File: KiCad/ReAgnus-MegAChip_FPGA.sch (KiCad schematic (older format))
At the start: 13 parts, among them J2 Conn_02x05_Odd_Even, J3 Conn_02x02_Odd_Even, U1 GW1NR-UV9LQ144P, U10 74LVC245A, U9 74LVC1GX04, Y1 CL=16pF

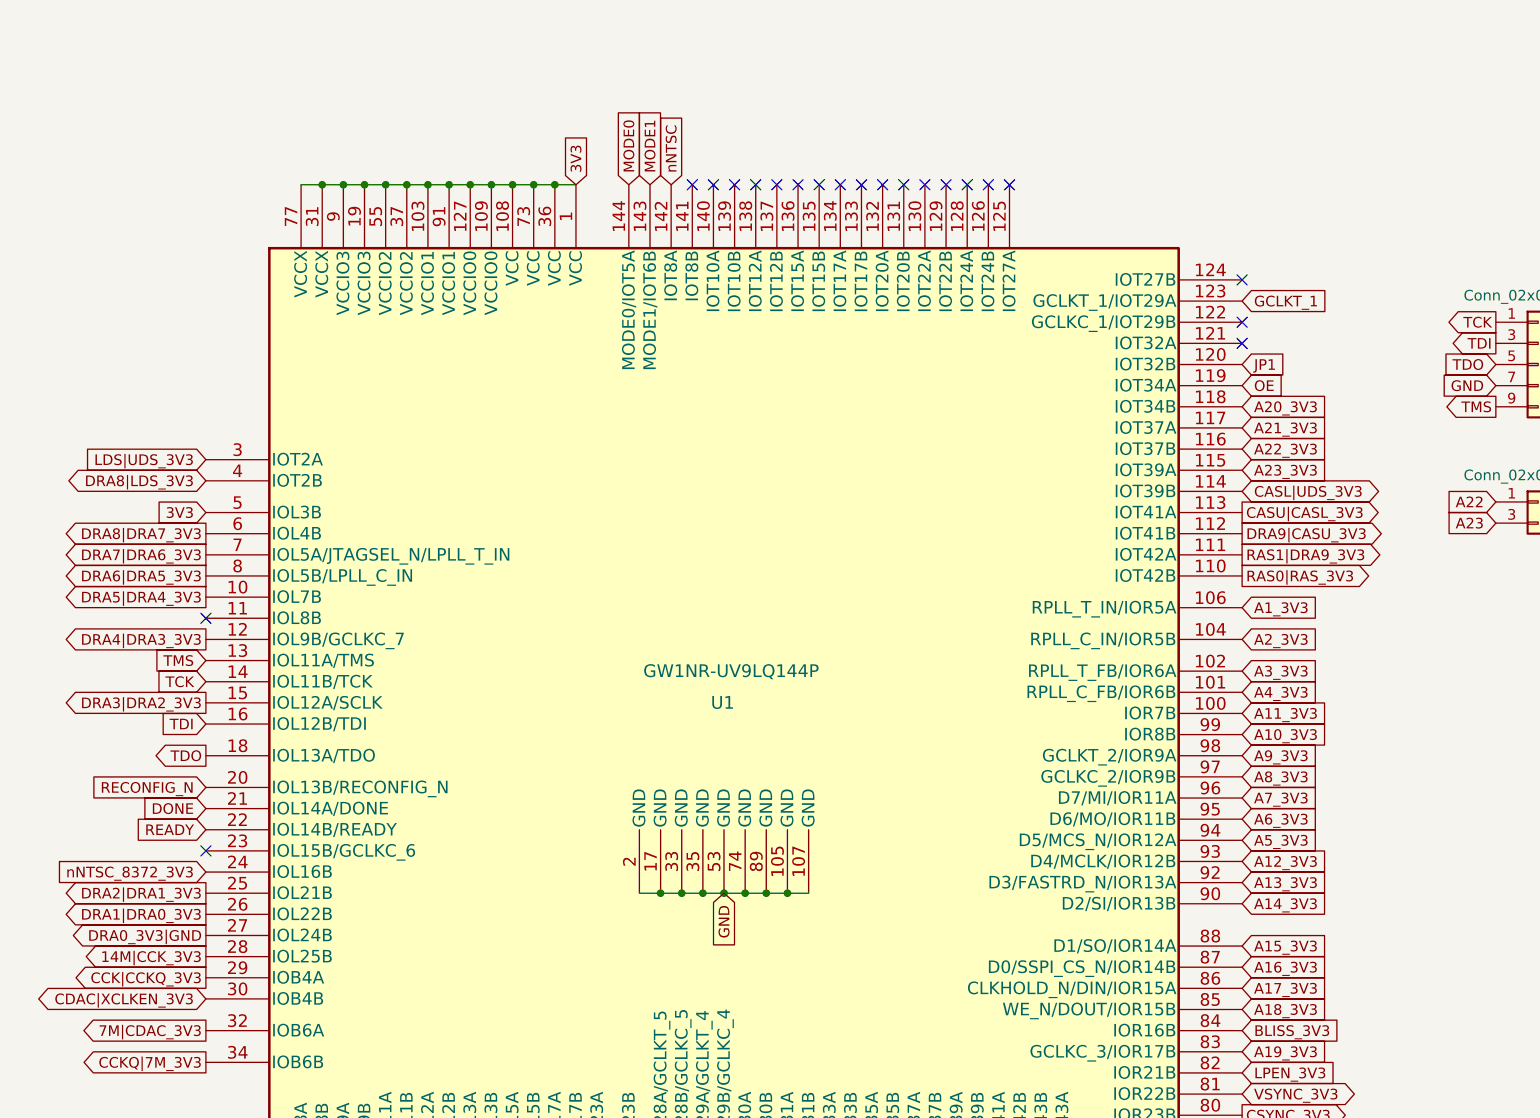
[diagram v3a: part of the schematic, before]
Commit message: Moved signals from bank 3 to bank 0
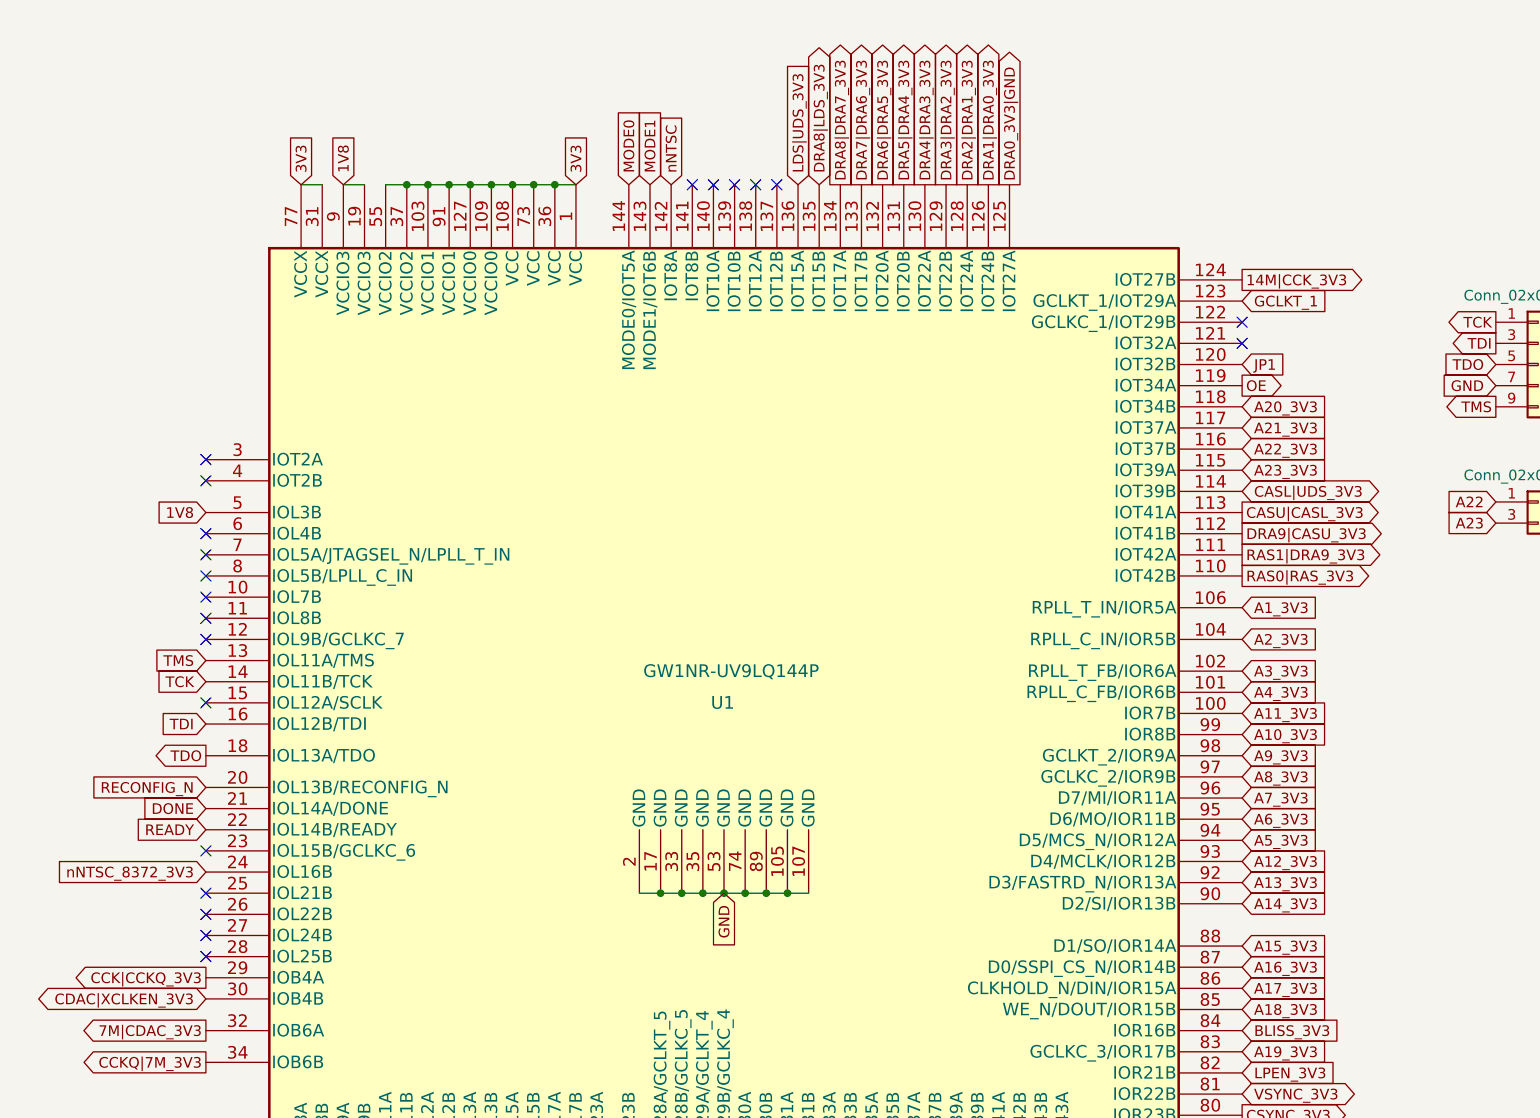
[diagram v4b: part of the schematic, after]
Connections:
- net 14M|CCK_3V3: now also U1.124 (IOT27B); no longer U1.28 (IOL25B)
- net 3V3: no longer U1.19 (VCCIO3), U1.5 (IOL3B), U1.9 (VCCIO3)
- net DRA0_3V3|GND: now also U1.125 (IOT27A); no longer U1.27 (IOL24B)
- net DRA1|DRA0_3V3: now also U1.126 (IOT24B); no longer U1.26 (IOL22B)
- net DRA2|DRA1_3V3: now also U1.128 (IOT24A); no longer U1.25 (IOL21B)
- net DRA3|DRA2_3V3: now also U1.129 (IOT22B); no longer U1.15 (IOL12A/SCLK)
- net DRA4|DRA3_3V3: now also U1.130 (IOT22A); no longer U1.12 (IOL9B/GCLKC_7)
- net DRA5|DRA4_3V3: now also U1.131 (IOT20B); no longer U1.10 (IOL7B)
- net DRA6|DRA5_3V3: now also U1.132 (IOT20A); no longer U1.8 (IOL5B/LPLL_C_IN)
- net DRA7|DRA6_3V3: now also U1.133 (IOT17B); no longer U1.7 (IOL5A/JTAGSEL_N/LPLL_T_IN)
- net DRA8|DRA7_3V3: now also U1.134 (IOT17A); no longer U1.6 (IOL4B)
- net DRA8|LDS_3V3: now also U1.135 (IOT15B); no longer U1.4 (IOT2B)
- net LDS|UDS_3V3: now also U1.136 (IOT15A); no longer U1.3 (IOT2A)
- new net 1V8: U1.19 (VCCIO3), U1.5 (IOL3B), U1.9 (VCCIO3)
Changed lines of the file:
@@
 Text GLabel 6400 2300 2    50   BiDi ~ 0
 CASL|UDS_3V3
-Text GLabel 1500 3000 0    50   Output ~ 0
+Text GLabel 4900 850  1    50   Output ~ 0
 DRA4|DRA3_3V3
-Text GLabel 1500 3300 0    50   Output ~ 0
+Text GLabel 5000 850  1    50   Output ~ 0
 DRA3|DRA2_3V3
-Text GLabel 1500 4200 0    50   Output ~ 0
+Text GLabel 5100 850  1    50   Output ~ 0
 DRA2|DRA1_3V3
-Text GLabel 1500 4300 0    50   Output ~ 0
+Text GLabel 5200 850  1    50   Output ~ 0
 DRA1|DRA0_3V3
-Text GLabel 1500 4400 0    50   Output ~ 0
+Text GLabel 5300 850  1    50   Output ~ 0
 DRA0_3V3|GND
 Text GLabel 2450 5750 3    50   Output ~ 0
@@
 Text GLabel 1500 4600 0    50   Output ~ 0
 CCK|CCKQ_3V3
-Text GLabel 1500 4500 0    50   Output ~ 0
+Text GLabel 6400 1300 2    50   Output ~ 0
 14M|CCK_3V3
 Text GLabel 1500 4850 0    50   Output ~ 0
@@
 Wire Wire Line
 	1950 850  2050 850
-Connection ~ 2050 850
-Wire Wire Line
-	2050 850  2150 850
-Connection ~ 2150 850
-Wire Wire Line
-	2150 850  2250 850
-Connection ~ 2250 850
-Wire Wire Line
-	2250 850  2350 850
-Connection ~ 2350 850
 Wire Wire Line
 	2350 850  2450 850
@@
 GND
 Text GLabel 1500 2400 0    50   Input ~ 0
-3V3
+1V8
 Text GLabel 3850 5750 3    50   Input ~ 0
 XCLK|A20_3V3
-Text GLabel 1500 2150 0    50   Input ~ 0
+Text GLabel 4300 850  1    50   Input ~ 0
 LDS|UDS_3V3
-Text GLabel 1500 2250 0    50   BiDi ~ 0
+Text GLabel 4400 850  1    50   BiDi ~ 0
 DRA8|LDS_3V3
-Text GLabel 1500 2500 0    50   Output ~ 0
+Text GLabel 4500 850  1    50   Output ~ 0
 DRA8|DRA7_3V3
-Text GLabel 1500 2600 0    50   Output ~ 0
+Text GLabel 4600 850  1    50   Output ~ 0
 DRA7|DRA6_3V3
-Text GLabel 1500 2700 0    50   Output ~ 0
+Text GLabel 4700 850  1    50   Output ~ 0
 DRA6|DRA5_3V3
-Text GLabel 1500 2800 0    50   Output ~ 0
+Text GLabel 4800 850  1    50   Output ~ 0
 DRA5|DRA4_3V3
 Text GLabel 9000 1450 3    50   Input ~ 0
@@
 	0    -1   -1   0
 $EndComp
-Text GLabel 6400 1800 2    50   Input ~ 0
+Text GLabel 6400 1800 2    50   Output ~ 0
 OE
 Wire Wire Line
@@
 Wire Wire Line
 	6350 7650 6450 7650
-NoConn ~ 6400 1600
-NoConn ~ 6400 1500
-NoConn ~ 6400 1300
-NoConn ~ 5300 850
-NoConn ~ 5200 850
-NoConn ~ 5100 850
-NoConn ~ 5000 850
-NoConn ~ 4900 850
-NoConn ~ 4800 850
-NoConn ~ 4700 850
-NoConn ~ 4600 850
-NoConn ~ 4500 850
-NoConn ~ 4400 850
-NoConn ~ 4300 850
 NoConn ~ 4200 850
 NoConn ~ 4100 850
@@
 NoConn ~ 1500 4000
 NoConn ~ 1500 2900
+NoConn ~ 1500 4500
+NoConn ~ 1500 4400
+NoConn ~ 1500 4300
+NoConn ~ 1500 4200
+Text GLabel 2150 850  1    50   Input ~ 0
+1V8
+Wire Wire Line
+	2150 850  2250 850
+Text GLabel 1950 850  1    50   Input ~ 0
+3V3
+NoConn ~ 1500 2150
+NoConn ~ 1500 2250
+NoConn ~ 1500 2500
+NoConn ~ 1500 2600
+NoConn ~ 1500 2700
+NoConn ~ 1500 3300
+NoConn ~ 1500 2800
+NoConn ~ 1500 3000
+NoConn ~ 6400 1500
+NoConn ~ 6400 1600
 $EndSCHEMATC

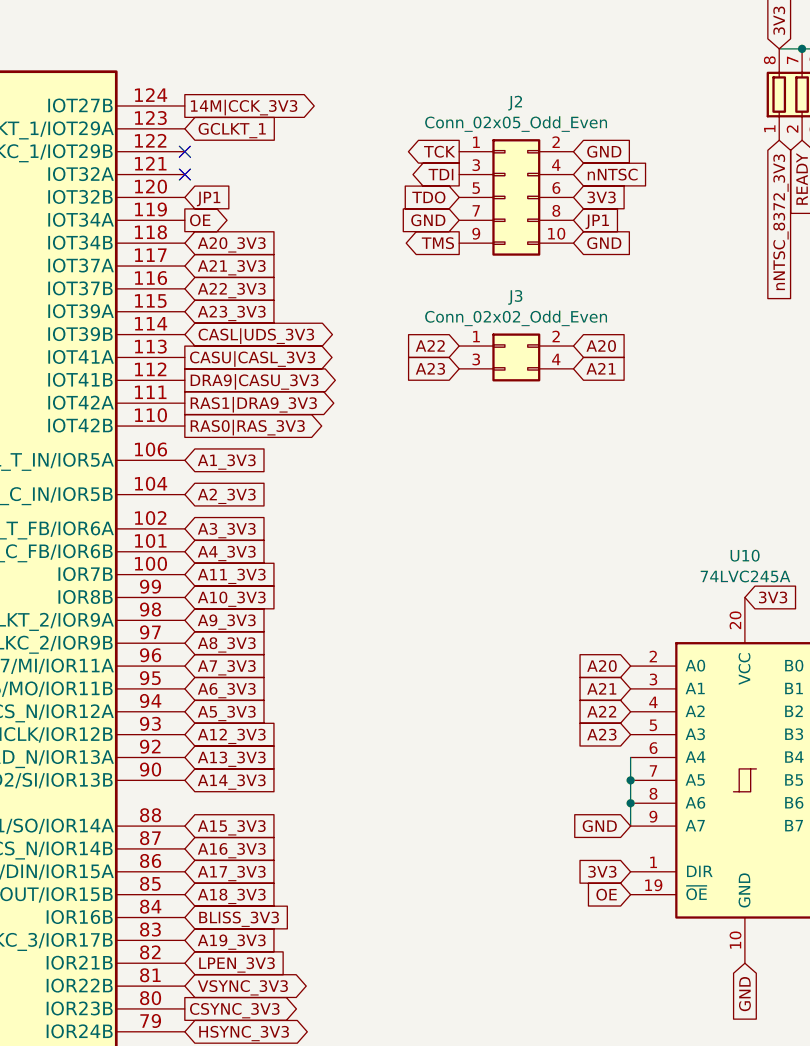
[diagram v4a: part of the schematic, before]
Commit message: Assigned DIR-signal to FPGA from U10 (74LVC245)
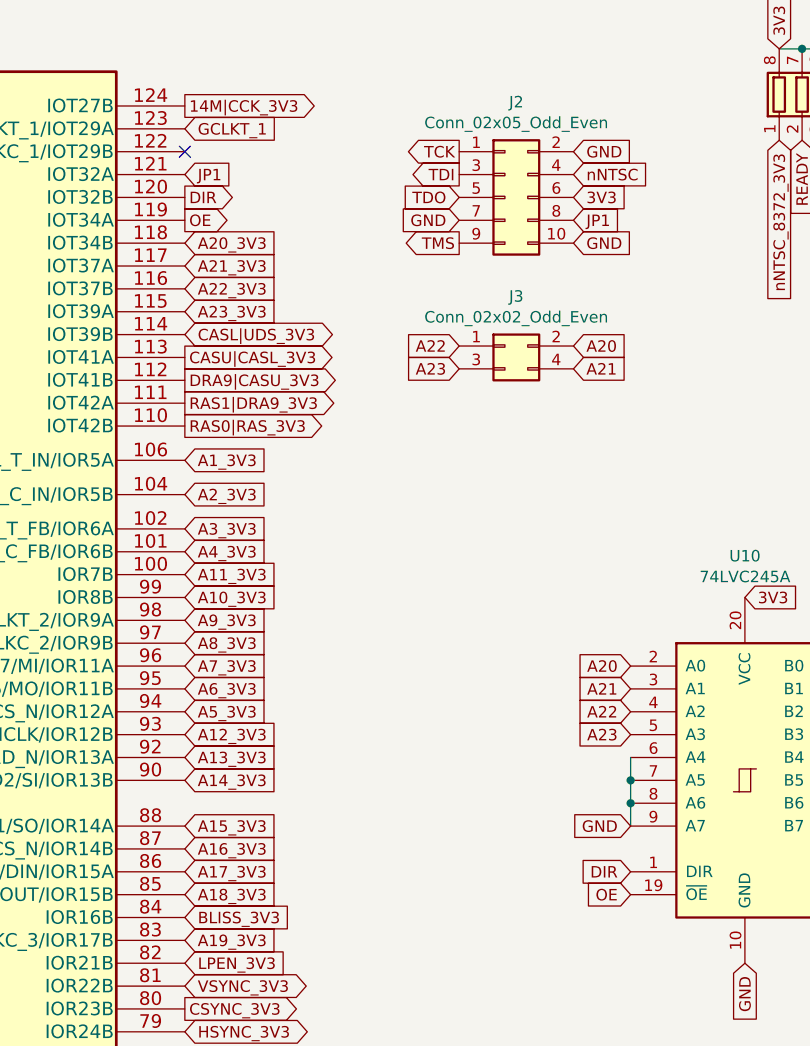
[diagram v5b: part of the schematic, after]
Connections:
- net 3V3: no longer U10.1 (DIR)
- net JP1: now also U1.121 (IOT32A); no longer U1.120 (IOT32B)
- new net DIR: U1.120 (IOT32B), U10.1 (DIR)
- no-connect marks 26 -> 25
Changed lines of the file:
@@
 3V3
 Text GLabel 8350 4650 0    50   Input ~ 0
-3V3
+DIR
 Wire Wire Line
 	8350 4150 8350 4250
@@
 Text GLabel 6450 7650 2    50   Output ~ 0
 GCLKT_1
-Text GLabel 6400 1700 2    50   Input ~ 0
+Text GLabel 6400 1600 2    50   Input ~ 0
 JP1
 Text GLabel 5850 7600 3    50   Input ~ 0
@@
 NoConn ~ 1500 3000
 NoConn ~ 6400 1500
-NoConn ~ 6400 1600
+Text GLabel 6400 1700 2    50   Output ~ 0
+DIR
 $EndSCHEMATC

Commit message: Added 1.8V LDO MCP1702T-1802E_CB to feed VCCIO3 (pSRAM) + inductor and decoupling and fixed routing, added pull-up resistor for JTAG TDO
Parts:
- added C28: 0.01uF, Capacitor_SMD:C_0603_1608Metric_Pad1.08x0.95mm_HandSolder, symbol Device:C_Small
- added C6: 0.1uF, Capacitor_SMD:C_0805_2012Metric_Pad1.18x1.45mm_HandSolder, symbol Device:C_Small
- added L1: 10uH, Inductor_SMD:L_0805_2012Metric_Pad1.05x1.20mm_HandSolder, symbol Device:L_Small
- added R5: 4.7k, Resistor_SMD:R_0603_1608Metric_Pad0.98x0.95mm_HandSolder, symbol Device:R_Small
- added U11: MCP1702T-1802E_CB, Package_TO_SOT_SMD:SOT-23_Handsoldering, symbol ReAgnus-MegAChip:MCP1702T-1802E_CB
- renumbered C28 to C29, C29 to C30
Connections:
- net labels added: VCCIO3
- wire segments 48 -> 55
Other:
- moved on the sheet: U10
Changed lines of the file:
@@
 Text GLabel 3700 850  1    50   Input ~ 0
 nNTSC
-Text GLabel 8350 3750 0    50   Input ~ 0
+Text GLabel 8800 3100 0    50   Input ~ 0
 A20
-Text GLabel 8350 3850 0    50   Input ~ 0
+Text GLabel 8800 3200 0    50   Input ~ 0
 A21
-Text GLabel 8350 3950 0    50   Input ~ 0
+Text GLabel 8800 3300 0    50   Input ~ 0
 A22
-Text GLabel 8350 4050 0    50   Input ~ 0
+Text GLabel 8800 3400 0    50   Input ~ 0
 A23
 Text GLabel 7600 2350 0    50   Input ~ 0
@@
 Text GLabel 8100 2350 2    50   Input ~ 0
 A20
-Text GLabel 8350 4450 0    50   Input ~ 0
-GND
-Text GLabel 8350 4750 0    50   Input ~ 0
+Text GLabel 8800 3800 0    50   Input ~ 0
+GND
+Text GLabel 8800 4100 0    50   Input ~ 0
 OE
-Text GLabel 9350 3750 2    50   Output ~ 0
+Text GLabel 9800 3100 2    50   Output ~ 0
 A20_3V3
-Text GLabel 9350 3850 2    50   Output ~ 0
+Text GLabel 9800 3200 2    50   Output ~ 0
 A21_3V3
-Text GLabel 9350 3950 2    50   Output ~ 0
+Text GLabel 9800 3300 2    50   Output ~ 0
 A22_3V3
-Text GLabel 9350 4050 2    50   Output ~ 0
+Text GLabel 9800 3400 2    50   Output ~ 0
 A23_3V3
 Text GLabel 6400 1900 2    50   Input ~ 0
@@
 L ReAgnus-MegAChip:74LVC245A U10
 U 1 1 6376E0A1
-P 8850 4250
-F 0 "U10" H 8850 5231 50  0000 C CNN
-F 1 "74LVC245A" H 8850 5140 50  0000 C CNN
-F 2 "Package_SO:TSSOP-20_4.4x6.5mm_P0.65mm" H 8850 4250 50  0001 C CNN
-F 3 "https://www.mouser.se/datasheet/2/916/74LVC_LVCH245A-1389000.pdf" H 8850 4250 50  0001 C CNN
-	1    8850 4250
-	1    0    0    -1
-$EndComp
-Text GLabel 8850 5050 3    50   Input ~ 0
-GND
-Text GLabel 8850 3450 2    50   Input ~ 0
-3V3
-Text GLabel 8350 4650 0    50   Input ~ 0
+P 9300 3600
+F 0 "U10" H 9300 4581 50  0000 C CNN
+F 1 "74LVC245A" H 9300 4490 50  0000 C CNN
+F 2 "Package_SO:TSSOP-20_4.4x6.5mm_P0.65mm" H 9300 3600 50  0001 C CNN
+F 3 "https://www.mouser.se/datasheet/2/916/74LVC_LVCH245A-1389000.pdf" H 9300 3600 50  0001 C CNN
+	1    9300 3600
+	1    0    0    -1
+$EndComp
+Text GLabel 9300 4400 3    50   Input ~ 0
+GND
+Text GLabel 9300 2800 2    50   Input ~ 0
+3V3
+Text GLabel 8800 4000 0    50   Input ~ 0
 DIR
 Wire Wire Line
-	8350 4150 8350 4250
-Connection ~ 8350 4250
-Wire Wire Line
-	8350 4250 8350 4350
-Connection ~ 8350 4350
-Wire Wire Line
-	8350 4350 8350 4450
-NoConn ~ 9350 4150
-NoConn ~ 9350 4250
-NoConn ~ 9350 4350
-NoConn ~ 9350 4450
+	8800 3500 8800 3600
+Connection ~ 8800 3600
+Wire Wire Line
+	8800 3600 8800 3700
+Connection ~ 8800 3700
+Wire Wire Line
+	8800 3700 8800 3800
+NoConn ~ 9800 3500
+NoConn ~ 9800 3600
+NoConn ~ 9800 3700
+NoConn ~ 9800 3800
 $Comp
 L ReAgnus-MegAChip:74LVC1GX04 U9
@@
 AR Path="/6383AF05" Ref="C?"  Part="1"
 AR Path="/632D3BDF/6383AF05" Ref="C?"  Part="1"
-AR Path="/632F104D/6383AF05" Ref="C28"  Part="1"
-F 0 "C28" V 4650 7350 50  0000 L CNN
+AR Path="/632F104D/6383AF05" Ref="C29"  Part="1"
+F 0 "C29" V 4650 7350 50  0000 L CNN
 F 1 "32pF" V 4750 7350 50  0000 L CNN
 F 2 "Capacitor_SMD:C_0603_1608Metric_Pad1.05x0.95mm_HandSolder" H 4500 7400 50  0001 C CNN
@@
 AR Path="/63835116" Ref="C?"  Part="1"
 AR Path="/632D3BDF/63835116" Ref="C?"  Part="1"
-AR Path="/632F104D/63835116" Ref="C29"  Part="1"
-F 0 "C29" V 4350 6850 50  0000 L CNN
+AR Path="/632F104D/63835116" Ref="C30"  Part="1"
+F 0 "C30" V 4350 6850 50  0000 L CNN
 F 1 "32pF" V 4250 6850 50  0000 L CNN
 F 2 "Capacitor_SMD:C_0603_1608Metric_Pad1.05x0.95mm_HandSolder" H 4500 6900 50  0001 C CNN
@@
 GND
 Text GLabel 1500 2400 0    50   Input ~ 0
-1V8
+VCCIO3
 Text GLabel 3850 5750 3    50   Input ~ 0
 XCLK|A20_3V3
@@
 	1    0    0    -1
 $EndComp
-Text GLabel 10200 1450 3    50   Input ~ 0
+Text GLabel 10700 1450 3    50   Input ~ 0
 TCK
 Text GLabel 9900 1450 3    50   Input ~ 0
@@
 	1    0    0    -1
 $EndComp
-Text GLabel 10100 1050 1    50   Input ~ 0
-3V3
-Text GLabel 9900 800  1    50   Input ~ 0
+Text GLabel 10200 1050 1    50   Input ~ 0
+3V3
+Text GLabel 9900 1050 1    50   Input ~ 0
 GND
 Wire Wire Line
 	9900 1050 10000 1050
-Wire Wire Line
-	9900 1050 9900 800
-Connection ~ 9900 1050
-Wire Wire Line
-	9900 800  10200 800
-Wire Wire Line
-	10200 800  10200 1050
 NoConn ~ 3500 5750
 Text GLabel 10100 1450 3    50   Input ~ 0
@@
 NoConn ~ 1500 4200
 Text GLabel 2150 850  1    50   Input ~ 0
-1V8
+VCCIO3
 Wire Wire Line
 	2150 850  2250 850
@@
 Text GLabel 6400 1700 2    50   Output ~ 0
 DIR
+$Comp
+L ReAgnus-MegAChip:MCP1702T-1802E_CB U11
+U 1 1 6677605D
+P 9300 5300
+F 0 "U11" H 9300 5615 50  0000 C CNN
+F 1 "MCP1702T-1802E_CB" H 9300 5524 50  0000 C CNN
+F 2 "Package_TO_SOT_SMD:SOT-23_Handsoldering" H 9700 5450 50  0001 L CNN
+F 3 "" H 9700 5350 50  0001 L CNN
+	1    9300 5300
+	1    0    0    -1
+$EndComp
+Text GLabel 9850 5250 2    50   Input ~ 0
+3V3
+Text GLabel 8350 5250 1    50   Input ~ 0
+GND
+Text GLabel 8750 5450 3    50   Output ~ 0
+1V8
+$Comp
+L Device:C_Small C?
+U 1 1 66807BC8
+P 8600 5350
+AR Path="/66807BC8" Ref="C?"  Part="1"
+AR Path="/632D3BDF/66807BC8" Ref="C?"  Part="1"
+AR Path="/632F104D/66807BC8" Ref="C6"  Part="1"
+F 0 "C6" H 8550 5200 50  0000 L CNN
+F 1 "0.1uF" H 8600 5100 50  0001 L CNN
+F 2 "Capacitor_SMD:C_0805_2012Metric_Pad1.18x1.45mm_HandSolder" H 8600 5350 50  0001 C CNN
+F 3 "~" H 8600 5350 50  0001 C CNN
+	1    8600 5350
+	1    0    0    -1
+$EndComp
+Wire Wire Line
+	8750 5350 8750 5450
+Wire Wire Line
+	8750 5450 8600 5450
+Connection ~ 8600 5450
+Wire Wire Line
+	8600 5450 8450 5450
+Connection ~ 8600 5250
+Wire Wire Line
+	8600 5250 8750 5250
+$Comp
+L Device:L_Small L1
+U 1 1 6686F06F
+P 8350 5450
+F 0 "L1" V 8300 5400 50  0000 L CNN
+F 1 "10uH" V 8450 5350 50  0000 L CNN
+F 2 "Inductor_SMD:L_0805_2012Metric_Pad1.05x1.20mm_HandSolder" H 8350 5450 50  0001 C CNN
+F 3 "~" H 8350 5450 50  0001 C CNN
+	1    8350 5450
+	0    1    1    0
+$EndComp
+$Comp
+L Device:C_Small C?
+U 1 1 668717A8
+P 8100 5350
+AR Path="/668717A8" Ref="C?"  Part="1"
+AR Path="/632D3BDF/668717A8" Ref="C?"  Part="1"
+AR Path="/632F104D/668717A8" Ref="C28"  Part="1"
+F 0 "C28" H 7850 5400 50  0000 L CNN
+F 1 "0.01uF" H 8100 5100 50  0001 L CNN
+F 2 "Capacitor_SMD:C_0603_1608Metric_Pad1.08x0.95mm_HandSolder" H 8100 5350 50  0001 C CNN
+F 3 "~" H 8100 5350 50  0001 C CNN
+	1    8100 5350
+	1    0    0    -1
+$EndComp
+Wire Wire Line
+	8250 5450 8100 5450
+Connection ~ 8100 5450
+Wire Wire Line
+	8100 5450 7950 5450
+Wire Wire Line
+	8100 5250 8600 5250
+Text GLabel 7950 5450 0    50   Output ~ 0
+VCCIO3
+Text GLabel 10200 1450 3    50   Input ~ 0
+TDO
+Wire Wire Line
+	10100 1050 10200 1050
+Text GLabel 10700 1050 1    50   Input ~ 0
+GND
+Wire Wire Line
+	10700 1350 10700 1450
+Wire Wire Line
+	10700 1050 10700 1150
+$Comp
+L Device:R_Small R5
+U 1 1 668F1087
+P 10700 1250
+F 0 "R5" V 10700 1250 50  0000 C CNN
+F 1 "4.7k" H 10550 1250 50  0000 C CNN
+F 2 "Resistor_SMD:R_0603_1608Metric_Pad0.98x0.95mm_HandSolder" H 10700 1250 50  0001 C CNN
+F 3 "~" H 10700 1250 50  0001 C CNN
+	1    10700 1250
+	-1   0    0    1
+$EndComp
 $EndSCHEMATC
